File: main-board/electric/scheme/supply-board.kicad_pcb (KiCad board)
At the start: 2 copper layers, 74 x 56 mm, 141 parts, among them K1 CONN_3, P1 PWR-IN, P10 TST, P11 TST, P12 PWR-IN, P13 CONN_4, P14 PWR-IN, P16 TST, P2 PWR-IN, P3 CONN_4, P4 cross board conn, P5 PWR-IN, P6 TST, P7 TST, P8 TST, P9 CONN_3X2, Q1 BC847, Q10 IRLML2502, Q11 IRLML2244, Q12 IRLML2244, Q2 BC847, Q3 BC847, Q4 IRLML2244, Q5 BC847, Q6 BC857, Q7 BC847, Q8 BC857, Q9 BC847, U1 NCP3063, U2 L293, U3 MINI-USB-B, X1 8MHz

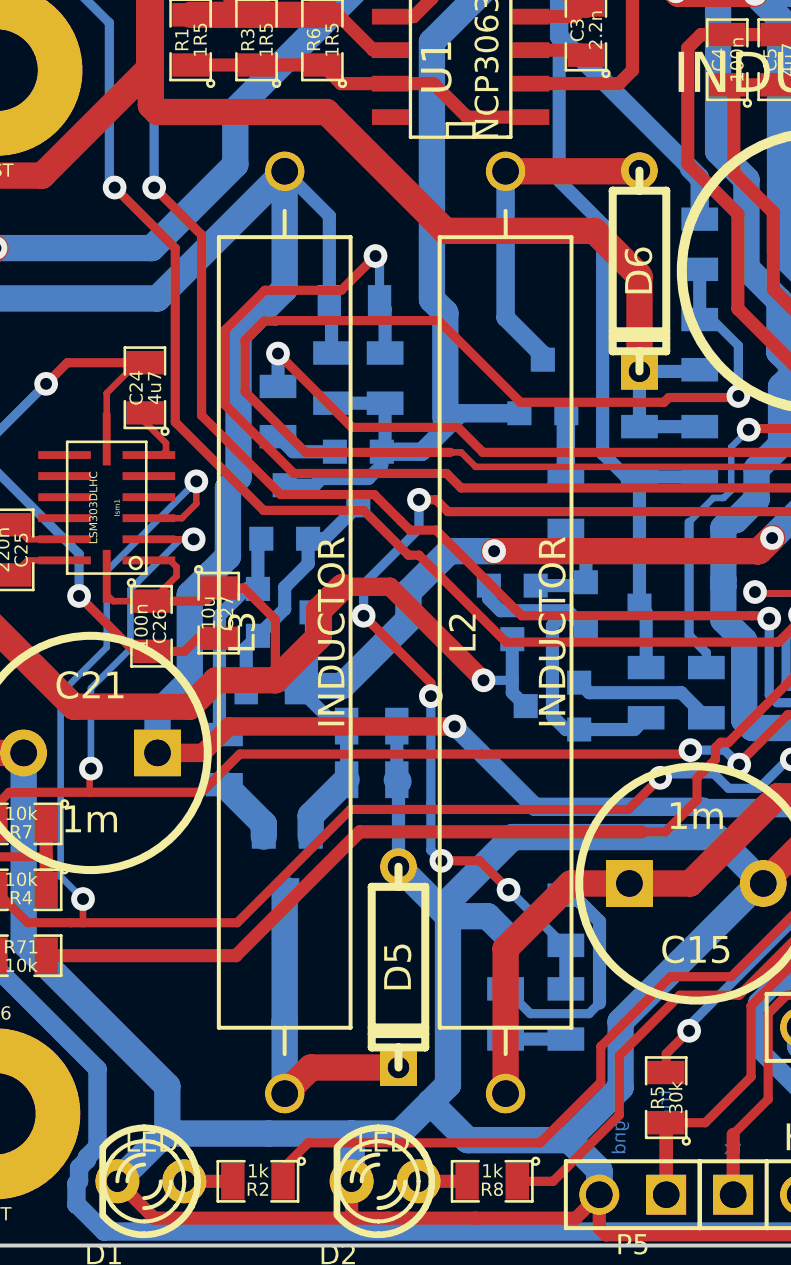
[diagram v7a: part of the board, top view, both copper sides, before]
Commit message: For boost and buck circuits made optional sot23/sot223 transistor packages.
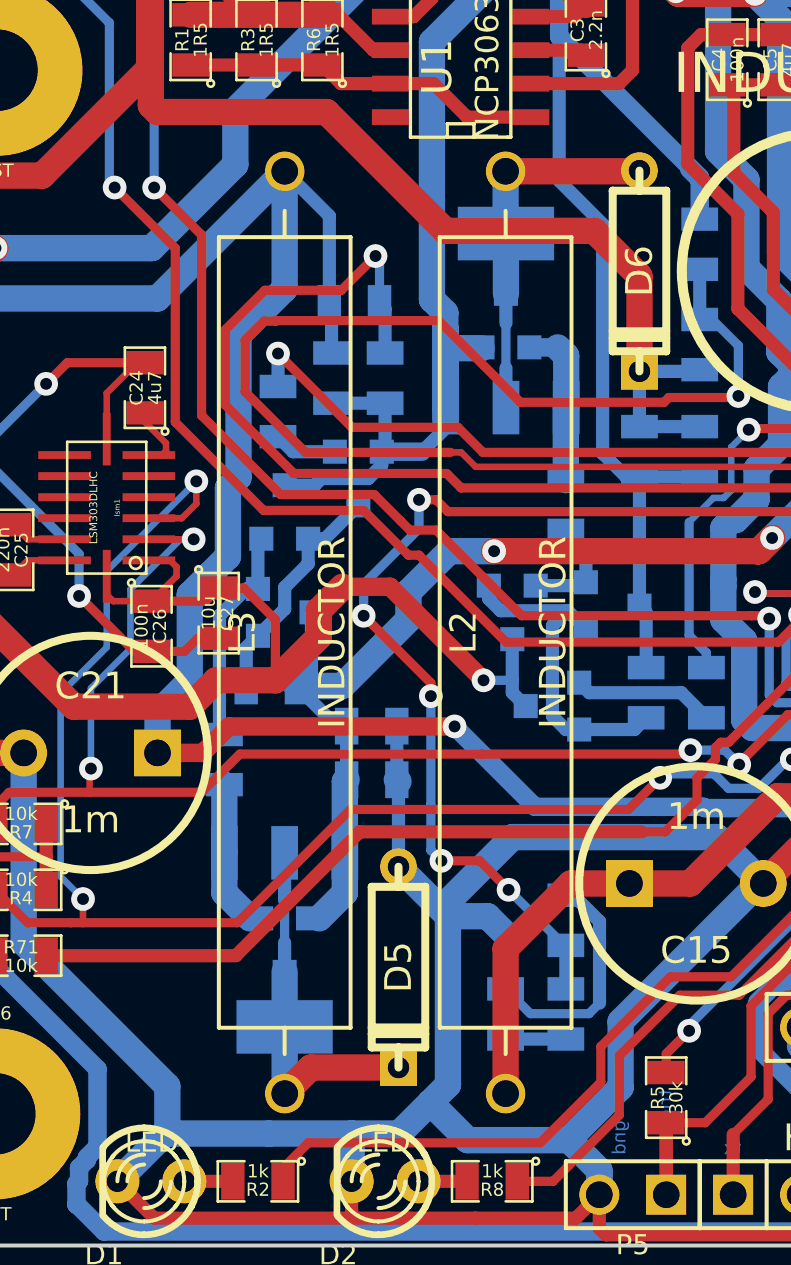
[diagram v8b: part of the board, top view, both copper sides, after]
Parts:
- added Q13: N-chan, sot-223, SOT223-GDSD, B.Cu at (167.4, 145.9)
- added Q14: P-chan, sot-223, SOT223-GDSD, B.Cu at (159.0, 169.4)
- moved Q11 3.10 mm to (159.0, 169.6)
- moved Q10 2.87 mm to (167.4, 145.9)
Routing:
- net N-0000055: track 2.55 -> 6.25 mm
- net /buck+: track 75.1 -> 78.0 mm
- net N-0000052: track 2.59 -> 5.47 mm
- net N-000007: track 12.7 -> 14.1 mm
- net N-0000056: track 12.8 -> 14.1 mm
